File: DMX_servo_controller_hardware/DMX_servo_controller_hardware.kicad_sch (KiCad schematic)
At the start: 18 parts

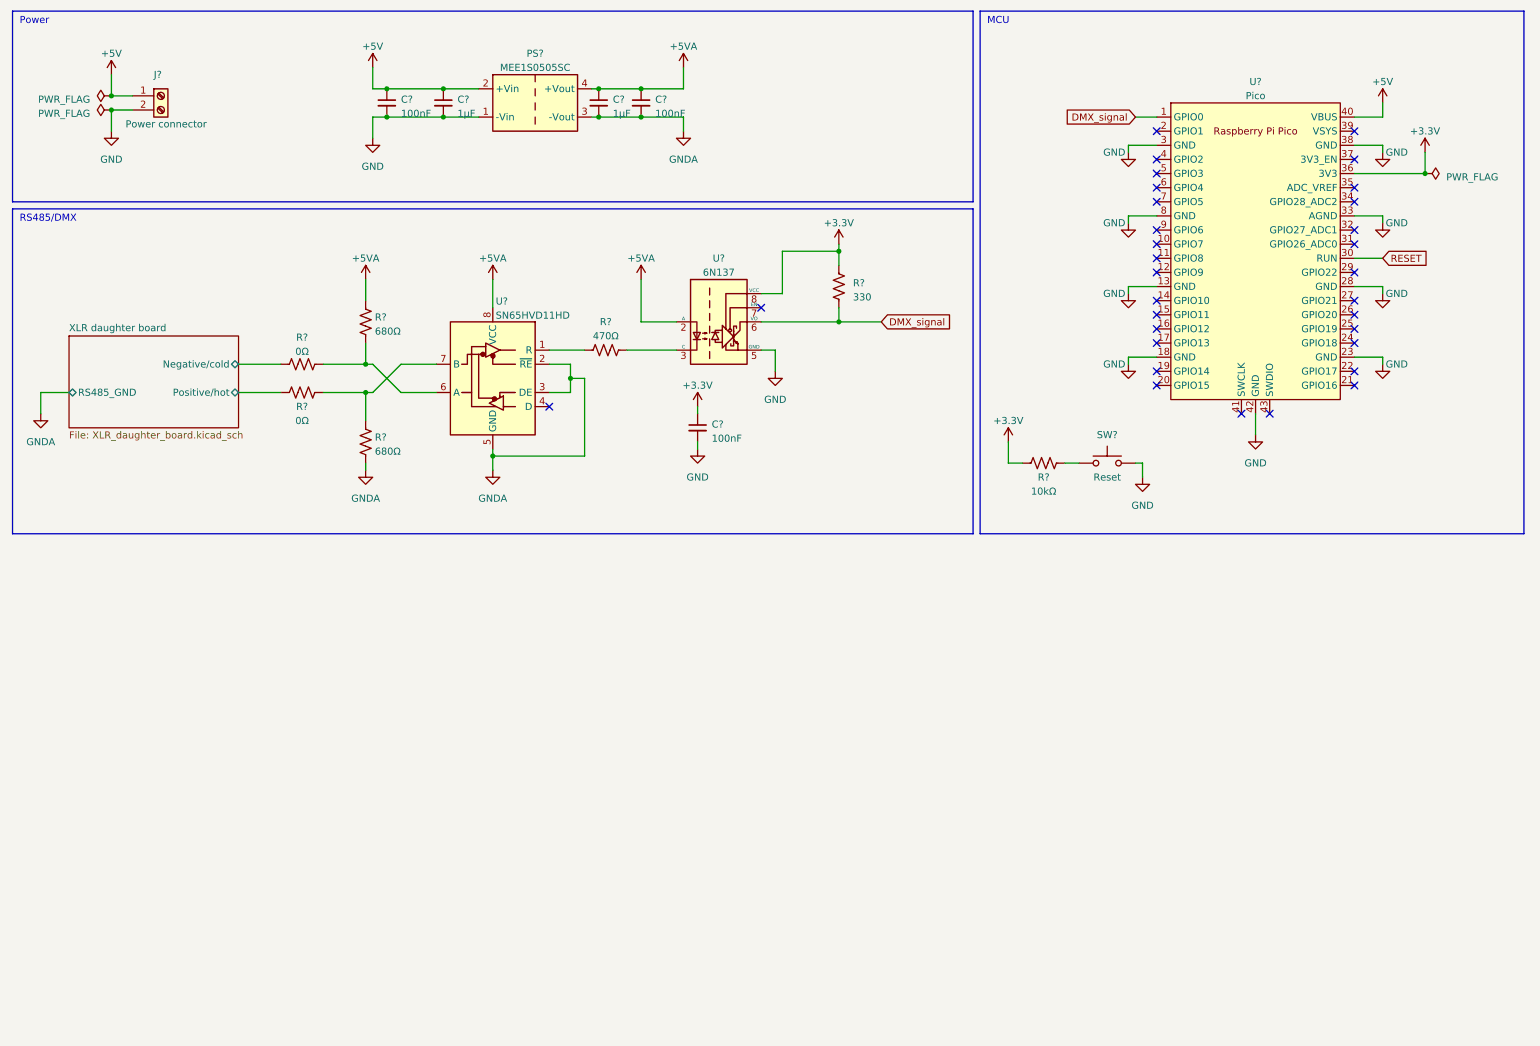
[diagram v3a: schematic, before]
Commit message: Adds connections for display
This also fixes the Reset switch (I was missing the signal on the
push button) and adds an external connector for the XLR signal (In case
we use the daughter board detached from the main board).
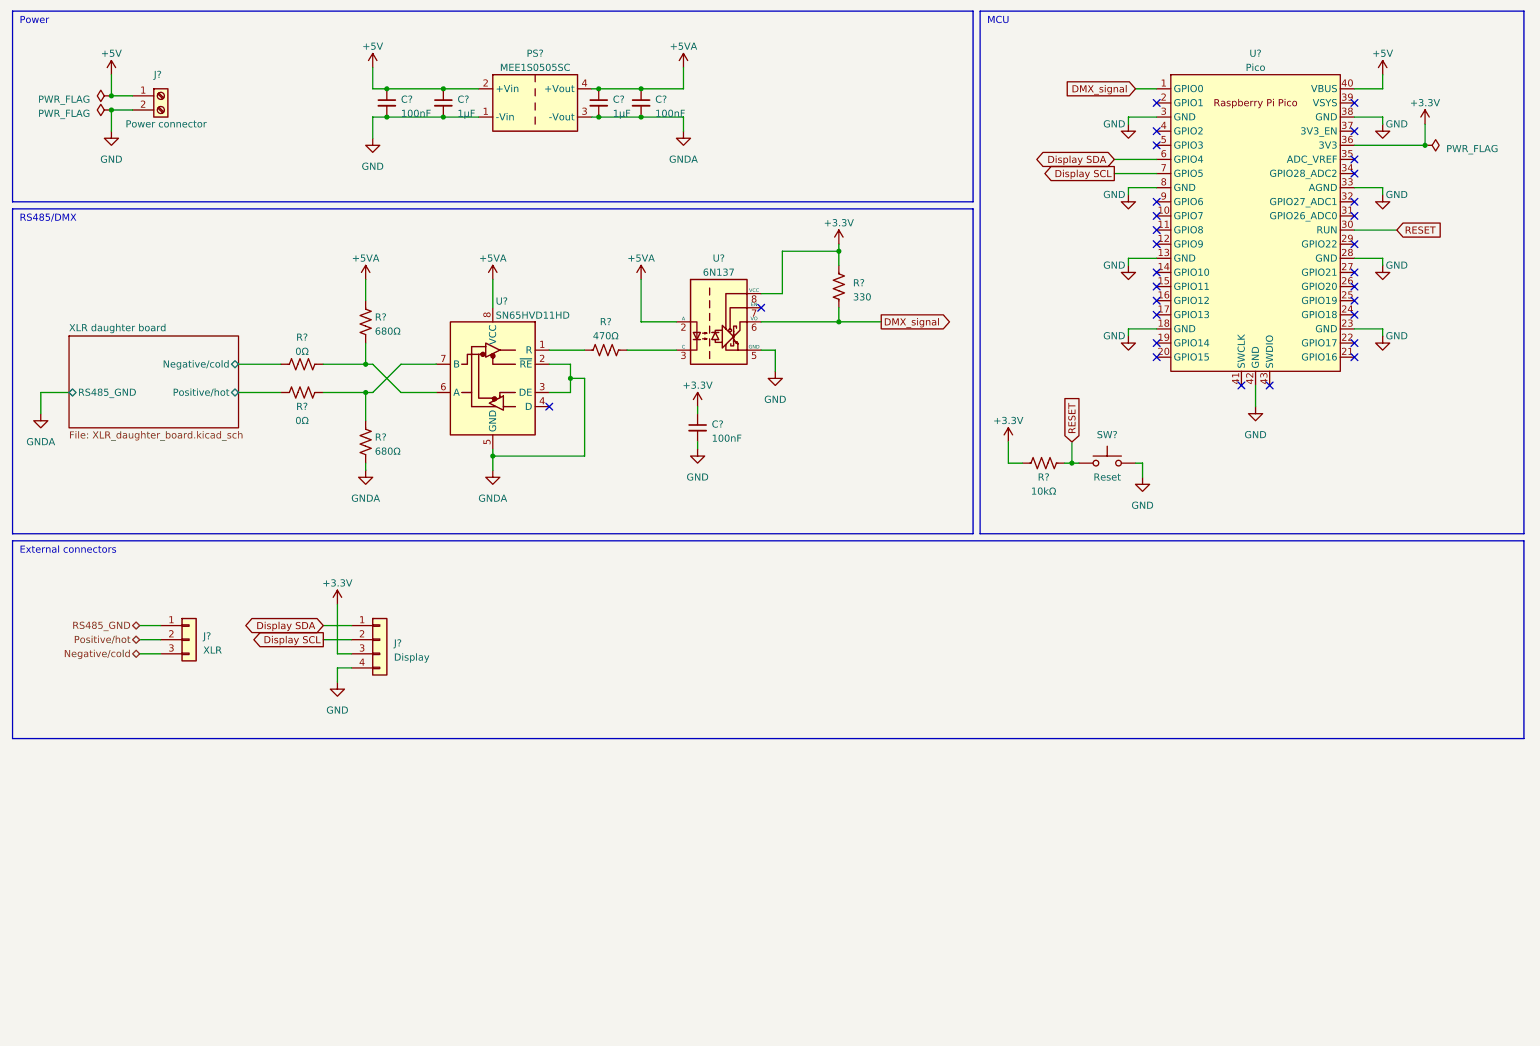
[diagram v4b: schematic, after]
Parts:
- added J?: Display, symbol Connector_Generic:Conn_01x04
- added J?: XLR, symbol Connector_Generic:Conn_01x03
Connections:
- net +3.3V: now also J?.3 (Pin_3)
- net GND: now also J?.4 (Pin_4)
- net RESET: now also R?.2, SW?.1
- net Display SDA: now reaches U?.6 (GPIO4)
- net Display SDA: now also J?.1 (Pin_1)
- net Display SCL: now reaches U?.7 (GPIO5)
- net Display SCL: now also J?.2 (Pin_2)
- new net Negative/cold: J?.3 (Pin_3)
- new net Positive/hot: J?.2 (Pin_2)
- new net RS485_GND: J?.1 (Pin_1)
- no-connect marks 32 -> 30
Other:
- note added: "External connectors"
- moved on the sheet: U?

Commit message: Adds connector for rotary encoder
The pinout needs to be reviewed when we decide on the actual module we
will use.
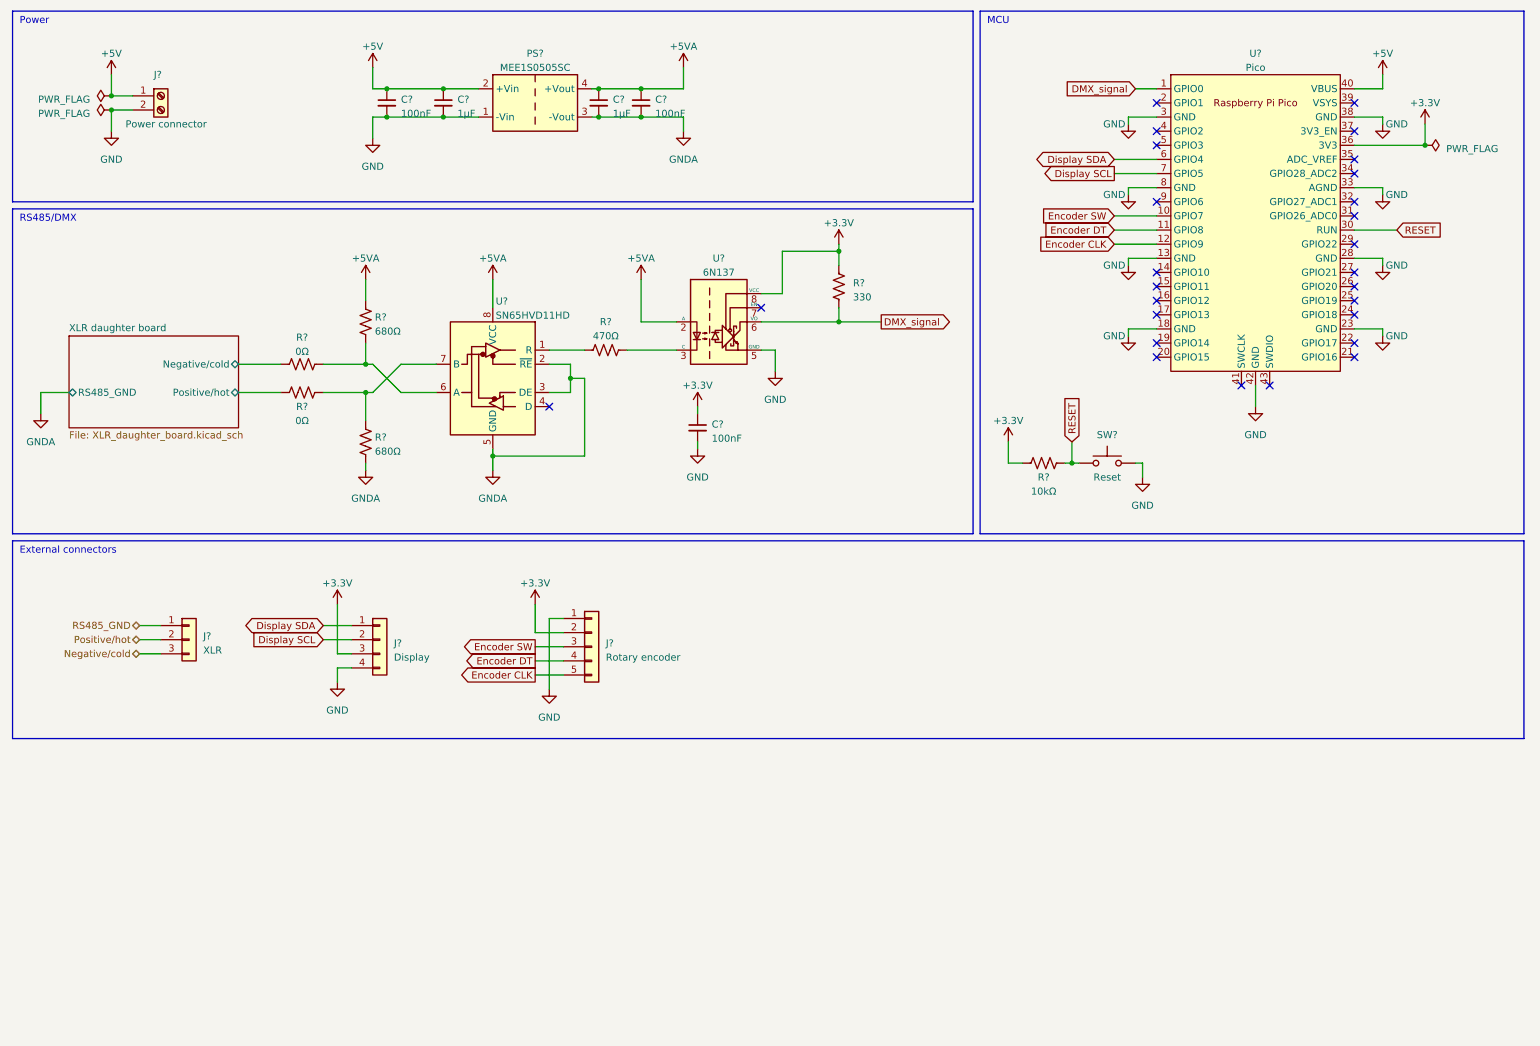
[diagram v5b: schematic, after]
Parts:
- added J?: Rotary encoder, symbol Connector_Generic:Conn_01x05
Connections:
- net +3.3V: now also J?.2 (Pin_2)
- net GND: now also J?.1 (Pin_1)
- net Encoder SW: now reaches U?.10 (GPIO7)
- net Encoder SW: now also J?.3 (Pin_3)
- net Encoder DT: now reaches U?.11 (GPIO8)
- net Encoder DT: now also J?.4 (Pin_4)
- net Encoder CLK: now reaches U?.12 (GPIO9)
- net Encoder CLK: now also J?.5 (Pin_5)
- no-connect marks 30 -> 27
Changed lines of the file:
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@@
   (no_connect (at 254 64.77))
   (no_connect (at 218.44 36.83))
-  (no_connect (at 218.44 52.07))
   (no_connect (at 254 49.53))
-  (no_connect (at 218.44 49.53))
   (no_connect (at 254 34.29))
   (no_connect (at 254 72.39))
@@
   (no_connect (at 254 54.61))
   (no_connect (at 254 74.93))
-  (no_connect (at 218.44 54.61))
   (no_connect (at 254 39.37))
   (no_connect (at 218.44 29.21))
@@
     (stroke (width 0) (type default))
   )
+  (wire (pts (xy 210.82 49.53) (xy 218.44 49.53))
+    (stroke (width 0) (type default))
+  )
   (wire (pts (xy 116.84 31.75) (xy 118.11 31.75))
     (stroke (width 0) (type default))
@@
     (stroke (width 0) (type default))
   )
+  (wire (pts (xy 210.82 54.61) (xy 218.44 54.61))
+    (stroke (width 0) (type default))
+  )
   (wire (pts (xy 76.2 72.39) (xy 76.2 76.2))
     (stroke (width 0) (type default))
@@
     (stroke (width 0) (type default))
   )
+  (wire (pts (xy 106.68 127) (xy 111.76 127))
+    (stroke (width 0) (type default))
+  )
   (wire (pts (xy 76.2 60.96) (xy 76.2 64.77))
     (stroke (width 0) (type default))
@@
     (stroke (width 0) (type default))
   )
+  (wire (pts (xy 109.22 134.62) (xy 109.22 121.92))
+    (stroke (width 0) (type default))
+  )
   (polyline (pts (xy 12.7 143.51) (xy 284.48 143.51))
     (stroke (width 0) (type default))
   )
+  (wire (pts (xy 106.68 129.54) (xy 111.76 129.54))
+    (stroke (width 0) (type default))
+  )
   (wire (pts (xy 53.34 81.28) (xy 60.96 81.28))
     (stroke (width 0) (type default))
@@
     (stroke (width 0) (type default))
   )
+  (wire (pts (xy 109.22 121.92) (xy 111.76 121.92))
+    (stroke (width 0) (type default))
+  )
   (wire (pts (xy 123.19 73.66) (xy 132.08 73.66))
     (stroke (width 0) (type default))
@@
     (stroke (width 0) (type default))
   )
+  (wire (pts (xy 106.68 124.46) (xy 111.76 124.46))
+    (stroke (width 0) (type default))
+  )
   (wire (pts (xy 161.29 55.88) (xy 161.29 58.42))
     (stroke (width 0) (type default))
@@
     (stroke (width 0) (type default))
   )
+  (wire (pts (xy 106.68 119.38) (xy 106.68 124.46))
+    (stroke (width 0) (type default))
+  )
   (wire (pts (xy 259.08 71.12) (xy 259.08 69.85))
     (stroke (width 0) (type default))
@@
     (stroke (width 0) (type default))
   )
+  (wire (pts (xy 106.68 132.08) (xy 111.76 132.08))
+    (stroke (width 0) (type default))
+  )
   (wire (pts (xy 76.2 93.98) (xy 76.2 95.25))
     (stroke (width 0) (type default))
@@
   )
   (wire (pts (xy 30.48 27.94) (xy 34.29 27.94))
+    (stroke (width 0) (type default))
+  )
+  (wire (pts (xy 210.82 52.07) (xy 218.44 52.07))
     (stroke (width 0) (type default))
   )
@@
     )
   )
+  (global_label "Encoder DT" (shape input) (at 210.82 52.07 180) (fields_autoplaced)
+    (effects (font (size 1.27 1.27)) (justify right))
+    (property "Intersheetrefs" "${INTERSHEET_REFS}" (at 197.1496 52.07 0)
+      (effects (font (size 1.27 1.27)) (justify right) hide)
+    )
+  )
   (global_label "DMX_signal" (shape output) (at 168.91 68.58 0) (fields_autoplaced)
     (effects (font (size 1.27 1.27)) (justify left))
@@
     )
   )
+  (global_label "Encoder SW" (shape output) (at 106.68 127 180) (fields_autoplaced)
+    (effects (font (size 1.27 1.27)) (justify right))
+    (property "Intersheetrefs" "${INTERSHEET_REFS}" (at 92.5863 127 0)
+      (effects (font (size 1.27 1.27)) (justify right) hide)
+    )
+  )
   (global_label "RESET" (shape input) (at 261.62 52.07 0) (fields_autoplaced)
     (effects (font (size 1.27 1.27)) (justify left))
@@
     )
   )
+  (global_label "Encoder CLK" (shape output) (at 106.68 132.08 180) (fields_autoplaced)
+    (effects (font (size 1.27 1.27)) (justify right))
+    (property "Intersheetrefs" "${INTERSHEET_REFS}" (at 91.6791 132.08 0)
+      (effects (font (size 1.27 1.27)) (justify right) hide)
+    )
+  )
+  (global_label "Encoder DT" (shape output) (at 106.68 129.54 180) (fields_autoplaced)
+    (effects (font (size 1.27 1.27)) (justify right))
+    (property "Intersheetrefs" "${INTERSHEET_REFS}" (at 93.0096 129.54 0)
+      (effects (font (size 1.27 1.27)) (justify right) hide)
+    )
+  )
   (global_label "Display SDA" (shape bidirectional) (at 210.82 39.37 180) (fields_autoplaced)
     (effects (font (size 1.27 1.27)) (justify right))
@@
     )
   )
+  (global_label "Encoder SW" (shape input) (at 210.82 49.53 180) (fields_autoplaced)
+    (effects (font (size 1.27 1.27)) (justify right))
+    (property "Intersheetrefs" "${INTERSHEET_REFS}" (at 196.7263 49.53 0)
+      (effects (font (size 1.27 1.27)) (justify right) hide)
+    )
+  )
   (global_label "Display SCL" (shape output) (at 210.82 41.91 180) (fields_autoplaced)
     (effects (font (size 1.27 1.27)) (justify right))
@@
     )
   )
-  (global_label "Display SCL" (shape output) (at 68.58 125.73 180) (fields_autoplaced)
+  (global_label "Display SCL" (shape input) (at 68.58 125.73 180) (fields_autoplaced)
     (effects (font (size 1.27 1.27)) (justify right))
     (property "Intersheetrefs" "${INTERSHEET_REFS}" (at 54.3653 125.73 0)
@@
     )
   )
+  (global_label "Encoder CLK" (shape input) (at 210.82 54.61 180) (fields_autoplaced)
+    (effects (font (size 1.27 1.27)) (justify right))
+    (property "Intersheetrefs" "${INTERSHEET_REFS}" (at 195.8191 54.61 0)
+      (effects (font (size 1.27 1.27)) (justify right) hide)
+    )
+  )
   (hierarchical_label "RS485_GND" (shape bidirectional) (at 35.56 123.19 180) (fields_autoplaced)
     (effects (font (size 1.27 1.27)) (justify right))
@@
         (path "/cd90393c-7fb4-4867-84b8-7df1a2bf6613"
           (reference "#PWR?") (unit 1)
+        )
+      )
+    )
+  )
+  (symbol (lib_id "power:GND") (at 109.22 134.62 0) (unit 1)
+    (in_bom yes) (on_board yes) (dnp no)
+    (property "Reference" "#PWR02" (at 109.22 140.97 0)
+      (effects (font (size 1.27 1.27)) hide)
+    )
+    (property "Value" "GND" (at 109.22 139.7 0)
+      (effects (font (size 1.27 1.27)))
+    )
+    (property "Footprint" "" (at 109.22 134.62 0)
+      (effects (font (size 1.27 1.27)) hide)
+    )
+    (property "Datasheet" "" (at 109.22 134.62 0)
+      (effects (font (size 1.27 1.27)) hide)
+    )
+    (pin "1")
+    (instances
+      (project "DMX_servo_controller_hardware"
+        (path "/cd90393c-7fb4-4867-84b8-7df1a2bf6613"
+          (reference "#PWR02") (unit 1)
         )
       )
@@
     )
   )
+  (symbol (lib_id "power:+3.3V") (at 106.68 119.38 0) (unit 1)
+    (in_bom yes) (on_board yes) (dnp no) (fields_autoplaced)
+    (property "Reference" "#PWR01" (at 106.68 123.19 0)
+      (effects (font (size 1.27 1.27)) hide)
+    )
+    (property "Value" "+3.3V" (at 106.68 115.57 0)
+      (effects (font (size 1.27 1.27)))
+    )
+    (property "Footprint" "" (at 106.68 119.38 0)
+      (effects (font (size 1.27 1.27)) hide)
+    )
+    (property "Datasheet" "" (at 106.68 119.38 0)
+      (effects (font (size 1.27 1.27)) hide)
+    )
+    (pin "1")
+    (instances
+      (project "DMX_servo_controller_hardware"
+        (path "/cd90393c-7fb4-4867-84b8-7df1a2bf6613"
+          (reference "#PWR01") (unit 1)
+        )
+      )
+    )
+  )
   (symbol (lib_id "power:+5V") (at 30.48 24.13 0) (unit 1)
     (in_bom yes) (on_board yes) (dnp no) (fields_autoplaced)
@@
         )
       )
+    )
+  )
+  (symbol (lib_id "Connector_Generic:Conn_01x05") (at 116.84 127 0) (unit 1)
+    (in_bom yes) (on_board yes) (dnp no) (fields_autoplaced)
+    (property "Reference" "J?" (at 119.38 126.365 0)
+      (effects (font (size 1.27 1.27)) (justify left))
+    )
+    (property "Value" "Rotary encoder" (at 119.38 128.905 0)
+      (effects (font (size 1.27 1.27)) (justify left))
+    )
+    (property "Footprint" "" (at 116.84 127 0)
+      (effects (font (size 1.27 1.27)) hide)
+    )
+    (property "Datasheet" "~" (at 116.84 127 0)
+      (effects (font (size 1.27 1.27)) hide)
+    )
+    (pin "1")
+    (pin "2")
+    (pin "3")
+    (pin "4")
+    (pin "5")
+    (instances
+      (project "DMX_servo_controller_hardware"
+        (path "/cd90393c-7fb4-4867-84b8-7df1a2bf6613"
+          (reference "J?") (unit 1)
+        )
+      )
